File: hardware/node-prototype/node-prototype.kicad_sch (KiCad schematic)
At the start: 0 parts

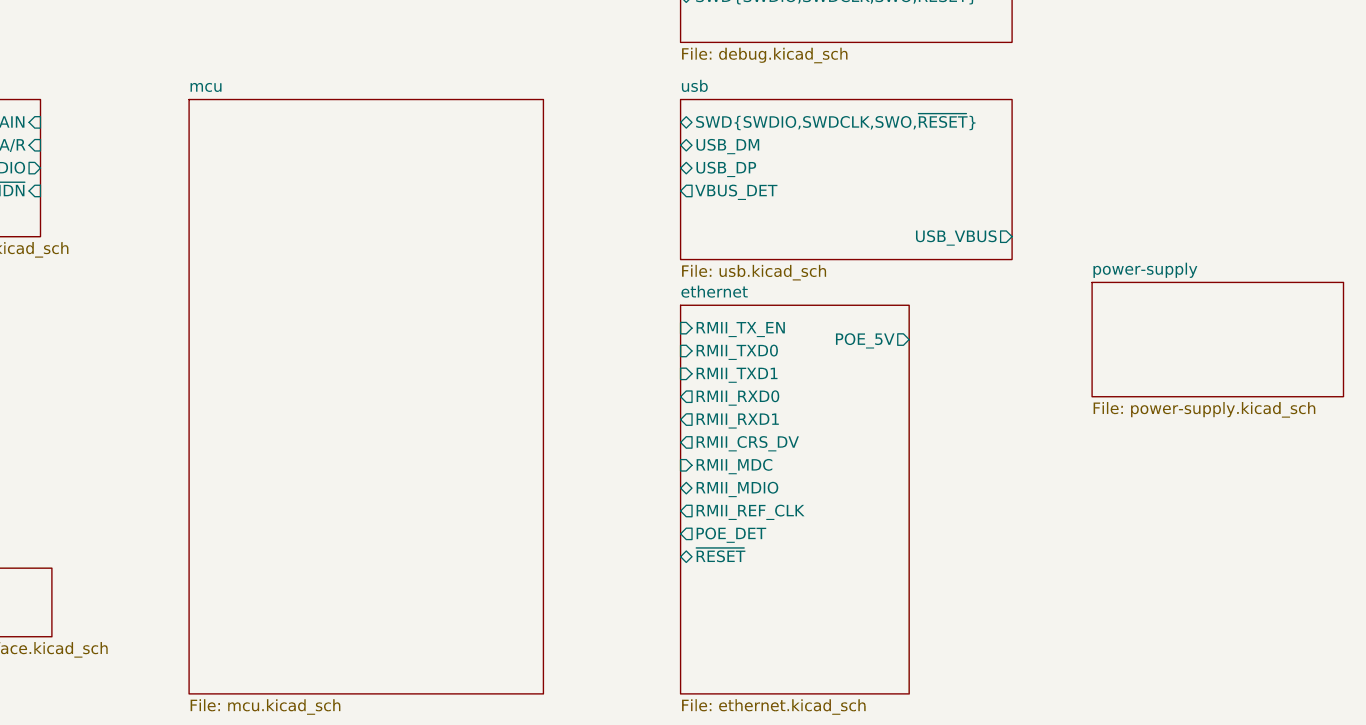
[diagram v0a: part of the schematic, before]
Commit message: Import labels in root sheet
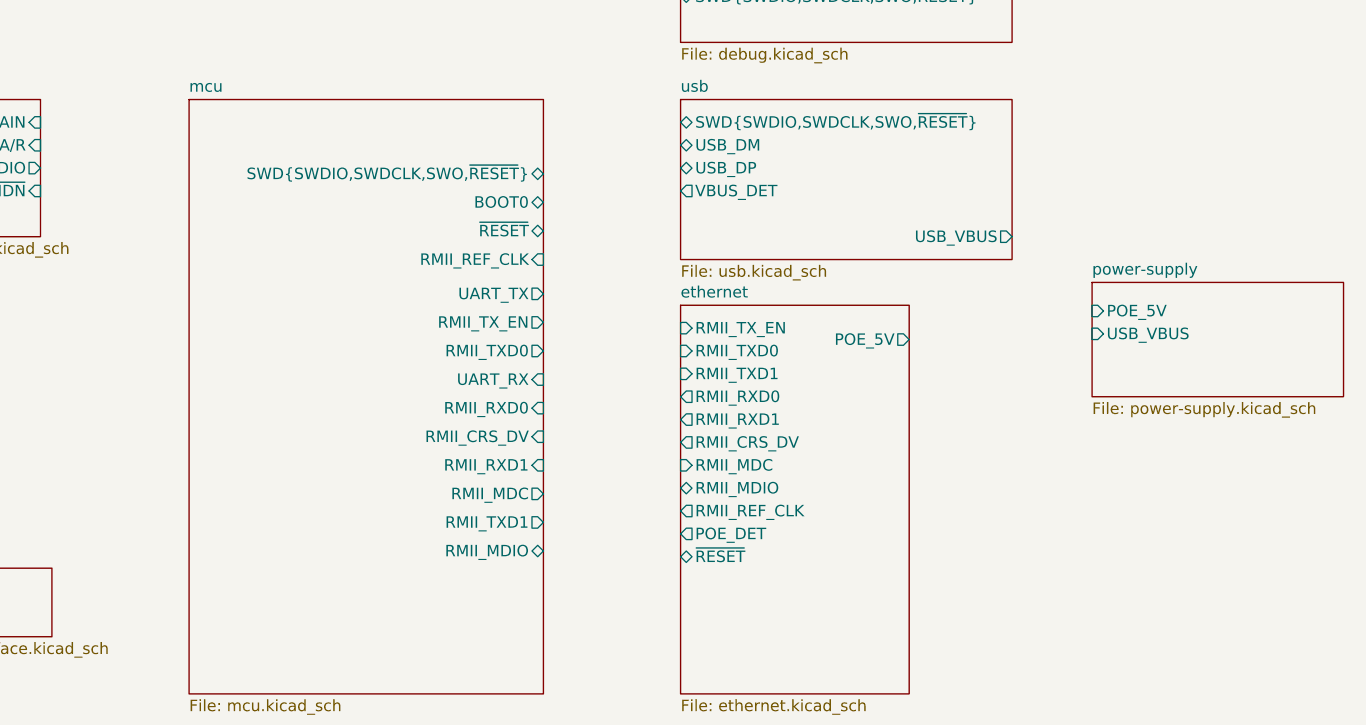
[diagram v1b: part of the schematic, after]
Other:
- sheet mcu ports: added BOOT0, RMII_CRS_DV, RMII_MDC, RMII_MDIO, RMII_REF_CLK, RMII_RXD0, RMII_RXD1, RMII_TXD0, RMII_TXD1, RMII_TX_EN, SWD{SWDIO,SWDCLK,SWO,~{RESET}}, UART_RX, UART_TX, ~{RESET}; removed none
- sheet power-supply ports: added POE_5V, USB_VBUS; removed none
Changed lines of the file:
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@@
       (effects (font (size 1.27 1.27)) (justify left top))
+    )
+    (pin "POE_5V" input (at 198.12 71.755 180)
+      (effects (font (size 1.27 1.27)) (justify left))
+    )
+    (pin "USB_VBUS" input (at 198.12 74.295 180)
+      (effects (font (size 1.27 1.27)) (justify left))
     )
     (instances
@@
       (effects (font (size 1.27 1.27)) (justify left top))
     )
+    (pin "SWD{SWDIO,SWDCLK,SWO,~{RESET}}" bidirectional (at 137.16 56.515 0)
+      (effects (font (size 1.27 1.27)) (justify right))
+    )
+    (pin "BOOT0" bidirectional (at 137.16 59.69 0)
+      (effects (font (size 1.27 1.27)) (justify right))
+    )
+    (pin "~{RESET}" bidirectional (at 137.16 62.865 0)
+      (effects (font (size 1.27 1.27)) (justify right))
+    )
+    (pin "RMII_REF_CLK" input (at 137.16 66.04 0)
+      (effects (font (size 1.27 1.27)) (justify right))
+    )
+    (pin "UART_TX" output (at 137.16 69.85 0)
+      (effects (font (size 1.27 1.27)) (justify right))
+    )
+    (pin "RMII_TX_EN" output (at 137.16 73.025 0)
+      (effects (font (size 1.27 1.27)) (justify right))
+    )
+    (pin "RMII_TXD0" output (at 137.16 76.2 0)
+      (effects (font (size 1.27 1.27)) (justify right))
+    )
+    (pin "UART_RX" input (at 137.16 79.375 0)
+      (effects (font (size 1.27 1.27)) (justify right))
+    )
+    (pin "RMII_RXD0" input (at 137.16 82.55 0)
+      (effects (font (size 1.27 1.27)) (justify right))
+    )
+    (pin "RMII_CRS_DV" input (at 137.16 85.725 0)
+      (effects (font (size 1.27 1.27)) (justify right))
+    )
+    (pin "RMII_RXD1" input (at 137.16 88.9 0)
+      (effects (font (size 1.27 1.27)) (justify right))
+    )
+    (pin "RMII_MDC" output (at 137.16 92.075 0)
+      (effects (font (size 1.27 1.27)) (justify right))
+    )
+    (pin "RMII_TXD1" output (at 137.16 95.25 0)
+      (effects (font (size 1.27 1.27)) (justify right))
+    )
+    (pin "RMII_MDIO" bidirectional (at 137.16 98.425 0)
+      (effects (font (size 1.27 1.27)) (justify right))
+    )
     (instances

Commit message: WIP on user interface
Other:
- sheet mcu ports: added USER_BTN, USER_LED_BLUE, USER_LED_RED; removed none
- sheet microphone ports: added MIC_AUDIO, MIC_A/R, MIC_GAIN, ~{MIC_SHDN}; removed AUDIO, A/R, GAIN, ~{SHDN}
- sheet user-interface ports: added BOOT0, USER_BTN, USER_LED_BLUE, USER_LED_RED, ~{RESET}; removed none
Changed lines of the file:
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@@
     (effects (font (size 1.27 1.27)) (justify left bottom))
   )
-  (sheet (at 63.5 100.33) (size 19.05 7.62) (fields_autoplaced)
+  (sheet (at 63.5 100.33) (size 19.05 29.845) (fields_autoplaced)
     (stroke (width 0.1524) (type solid))
     (fill (color 0 0 0 0.0000))
@@
       (effects (font (size 1.27 1.27)) (justify left bottom))
     )
-    (property "Sheetfile" "user-interface.kicad_sch" (at 63.5 108.5346 0)
-      (effects (font (size 1.27 1.27)) (justify left top))
+    (property "Sheetfile" "user-interface.kicad_sch" (at 63.5 130.7596 0)
+      (effects (font (size 1.27 1.27)) (justify left top))
+    )
+    (pin "BOOT0" output (at 82.55 107.315 0)
+      (effects (font (size 1.27 1.27)) (justify right))
+    )
+    (pin "USER_LED_RED" input (at 82.55 119.38 0)
+      (effects (font (size 1.27 1.27)) (justify right))
+    )
+    (pin "USER_BTN" output (at 82.55 109.855 0)
+      (effects (font (size 1.27 1.27)) (justify right))
+    )
+    (pin "USER_LED_BLUE" input (at 82.55 116.84 0)
+      (effects (font (size 1.27 1.27)) (justify right))
+    )
+    (pin "~{RESET}" output (at 82.55 104.775 0)
+      (effects (font (size 1.27 1.27)) (justify right))
     )
     (instances
@@
     )
   )
-  (sheet (at 60.96 48.26) (size 20.32 15.24) (fields_autoplaced)
-    (stroke (width 0.1524) (type solid))
-    (fill (color 0 0 0 0.0000))
-    (property "Sheetname" "microphone" (at 60.96 47.5484 0)
-      (effects (font (size 1.27 1.27)) (justify left bottom))
-    )
-    (property "Sheetfile" "microphone.kicad_sch" (at 60.96 64.0846 0)
-      (effects (font (size 1.27 1.27)) (justify left top))
-    )
-    (pin "GAIN" input (at 81.28 50.8 0)
-      (effects (font (size 1.27 1.27)) (justify right))
-    )
-    (pin "A{slash}R" input (at 81.28 53.34 0)
-      (effects (font (size 1.27 1.27)) (justify right))
-    )
-    (pin "AUDIO" output (at 81.28 55.88 0)
-      (effects (font (size 1.27 1.27)) (justify right))
-    )
-    (pin "~{SHDN}" input (at 81.28 58.42 0)
-      (effects (font (size 1.27 1.27)) (justify right))
+  (sheet (at 62.23 46.99) (size 20.32 38.1) (fields_autoplaced)
+    (stroke (width 0.1524) (type solid))
+    (fill (color 0 0 0 0.0000))
+    (property "Sheetname" "microphone" (at 62.23 46.2784 0)
+      (effects (font (size 1.27 1.27)) (justify left bottom))
+    )
+    (property "Sheetfile" "microphone.kicad_sch" (at 62.23 85.6746 0)
+      (effects (font (size 1.27 1.27)) (justify left top))
+    )
+    (pin "MIC_GAIN" input (at 62.23 52.07 180)
+      (effects (font (size 1.27 1.27)) (justify left))
+    )
+    (pin "MIC_AUDIO" output (at 62.23 49.53 180)
+      (effects (font (size 1.27 1.27)) (justify left))
+    )
+    (pin "~{MIC_SHDN}" input (at 62.23 54.61 180)
+      (effects (font (size 1.27 1.27)) (justify left))
+    )
+    (pin "MIC_A{slash}R" input (at 62.23 57.15 180)
+      (effects (font (size 1.27 1.27)) (justify left))
     )
     (instances
@@
       (effects (font (size 1.27 1.27)) (justify left top))
     )
-    (pin "SWD{SWDIO,SWDCLK,SWO,~{RESET}}" bidirectional (at 137.16 56.515 0)
-      (effects (font (size 1.27 1.27)) (justify right))
-    )
-    (pin "BOOT0" bidirectional (at 137.16 59.69 0)
-      (effects (font (size 1.27 1.27)) (justify right))
-    )
-    (pin "~{RESET}" bidirectional (at 137.16 62.865 0)
-      (effects (font (size 1.27 1.27)) (justify right))
-    )
-    (pin "RMII_REF_CLK" input (at 137.16 66.04 0)
-      (effects (font (size 1.27 1.27)) (justify right))
-    )
-    (pin "UART_TX" output (at 137.16 69.85 0)
-      (effects (font (size 1.27 1.27)) (justify right))
-    )
-    (pin "RMII_TX_EN" output (at 137.16 73.025 0)
-      (effects (font (size 1.27 1.27)) (justify right))
-    )
-    (pin "RMII_TXD0" output (at 137.16 76.2 0)
-      (effects (font (size 1.27 1.27)) (justify right))
-    )
-    (pin "UART_RX" input (at 137.16 79.375 0)
-      (effects (font (size 1.27 1.27)) (justify right))
-    )
-    (pin "RMII_RXD0" input (at 137.16 82.55 0)
-      (effects (font (size 1.27 1.27)) (justify right))
-    )
-    (pin "RMII_CRS_DV" input (at 137.16 85.725 0)
-      (effects (font (size 1.27 1.27)) (justify right))
-    )
-    (pin "RMII_RXD1" input (at 137.16 88.9 0)
-      (effects (font (size 1.27 1.27)) (justify right))
-    )
-    (pin "RMII_MDC" output (at 137.16 92.075 0)
-      (effects (font (size 1.27 1.27)) (justify right))
-    )
-    (pin "RMII_TXD1" output (at 137.16 95.25 0)
-      (effects (font (size 1.27 1.27)) (justify right))
-    )
-    (pin "RMII_MDIO" bidirectional (at 137.16 98.425 0)
-      (effects (font (size 1.27 1.27)) (justify right))
-    )
+    (pin "SWD{SWDIO,SWDCLK,SWO,~{RESET}}" bidirectional (at 137.16 73.66 0)
+      (effects (font (size 1.27 1.27)) (justify right))
+    )
+    (pin "BOOT0" input (at 137.16 51.435 0)
+      (effects (font (size 1.27 1.27)) (justify right))
+    )
+    (pin "~{RESET}" input (at 137.16 54.61 0)
+      (effects (font (size 1.27 1.27)) (justify right))
+    )
+    (pin "RMII_REF_CLK" input (at 137.16 76.2 0)
+      (effects (font (size 1.27 1.27)) (justify right))
+    )
+    (pin "UART_TX" output (at 137.16 80.01 0)
+      (effects (font (size 1.27 1.27)) (justify right))
+    )
+    (pin "RMII_TX_EN" output (at 137.16 83.185 0)
+      (effects (font (size 1.27 1.27)) (justify right))
+    )
+    (pin "RMII_TXD0" output (at 137.16 86.36 0)
+      (effects (font (size 1.27 1.27)) (justify right))
+    )
+    (pin "UART_RX" input (at 137.16 89.535 0)
+      (effects (font (size 1.27 1.27)) (justify right))
+    )
+    (pin "RMII_RXD0" input (at 137.16 92.71 0)
+      (effects (font (size 1.27 1.27)) (justify right))
+    )
+    (pin "RMII_CRS_DV" input (at 137.16 95.885 0)
+      (effects (font (size 1.27 1.27)) (justify right))
+    )
+    (pin "RMII_RXD1" input (at 137.16 99.06 0)
+      (effects (font (size 1.27 1.27)) (justify right))
+    )
+    (pin "RMII_MDC" output (at 137.16 102.235 0)
+      (effects (font (size 1.27 1.27)) (justify right))
+    )
+    (pin "RMII_TXD1" output (at 137.16 105.41 0)
+      (effects (font (size 1.27 1.27)) (justify right))
+    )
+    (pin "RMII_MDIO" bidirectional (at 137.16 108.585 0)
+      (effects (font (size 1.27 1.27)) (justify right))
+    )
+    (pin "USER_BTN" input (at 137.16 57.15 0)
+      (effects (font (size 1.27 1.27)) (justify right))
+    )
+    (pin "USER_LED_BLUE" output (at 137.16 62.23 0)
+      (effects (font (size 1.27 1.27)) (justify right))
+    )
+    (pin "USER_LED_RED" output (at 137.16 65.405 0)
+      (effects (font (size 1.27 1.27)) (justify right))
+    )

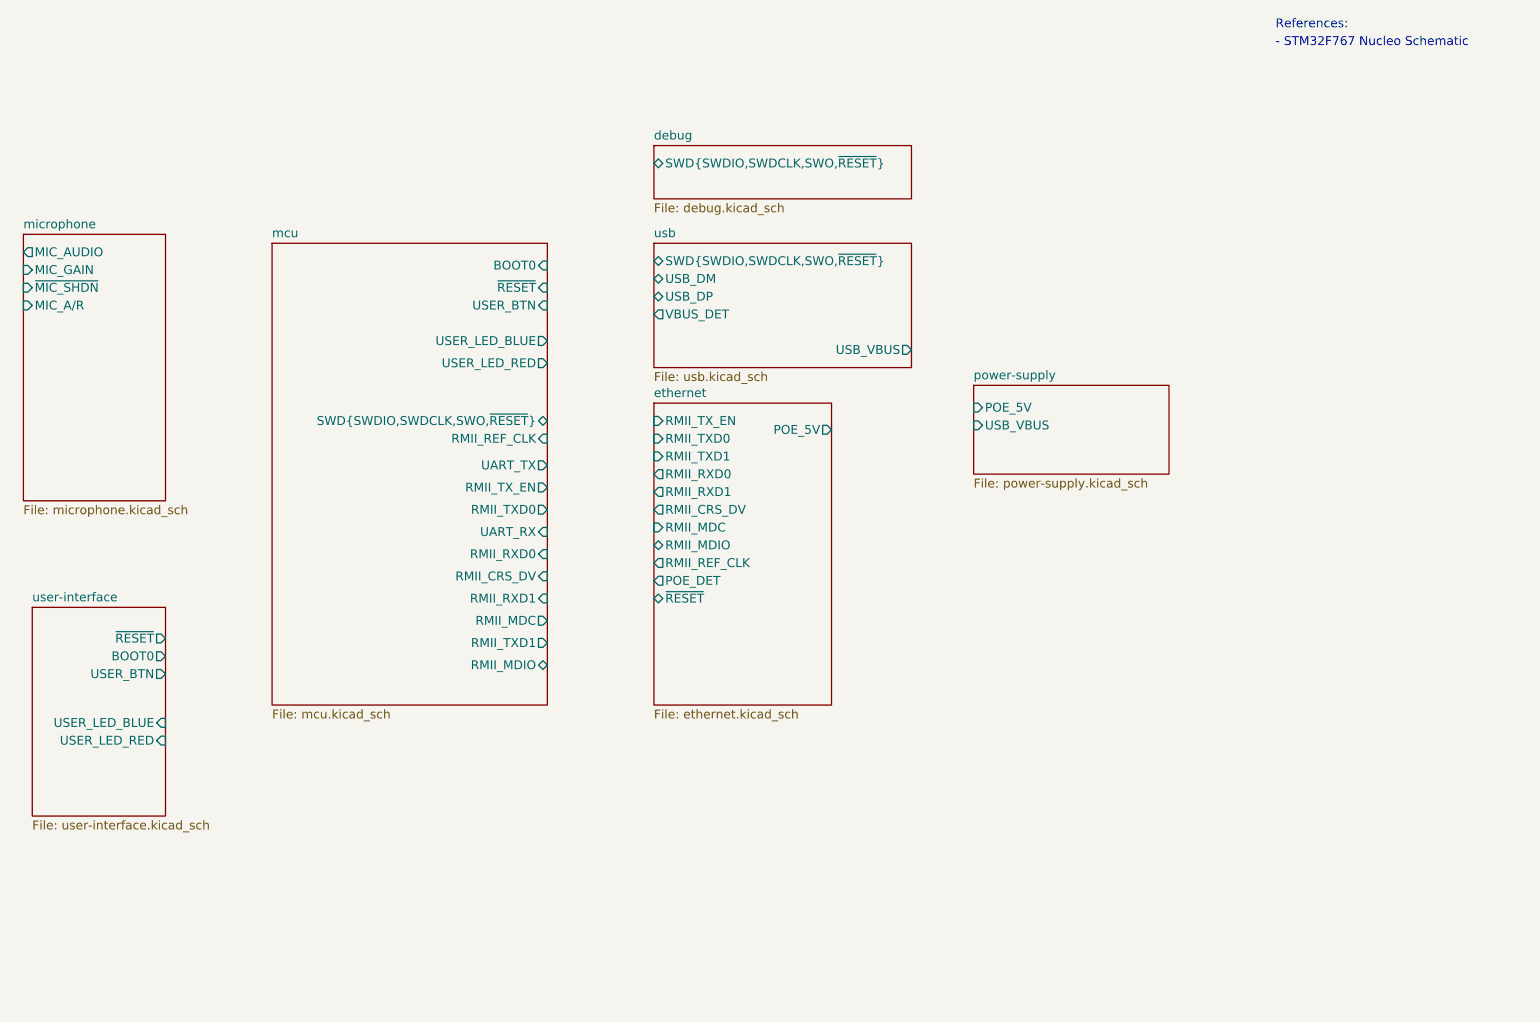
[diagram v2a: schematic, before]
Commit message: Plug schematic together
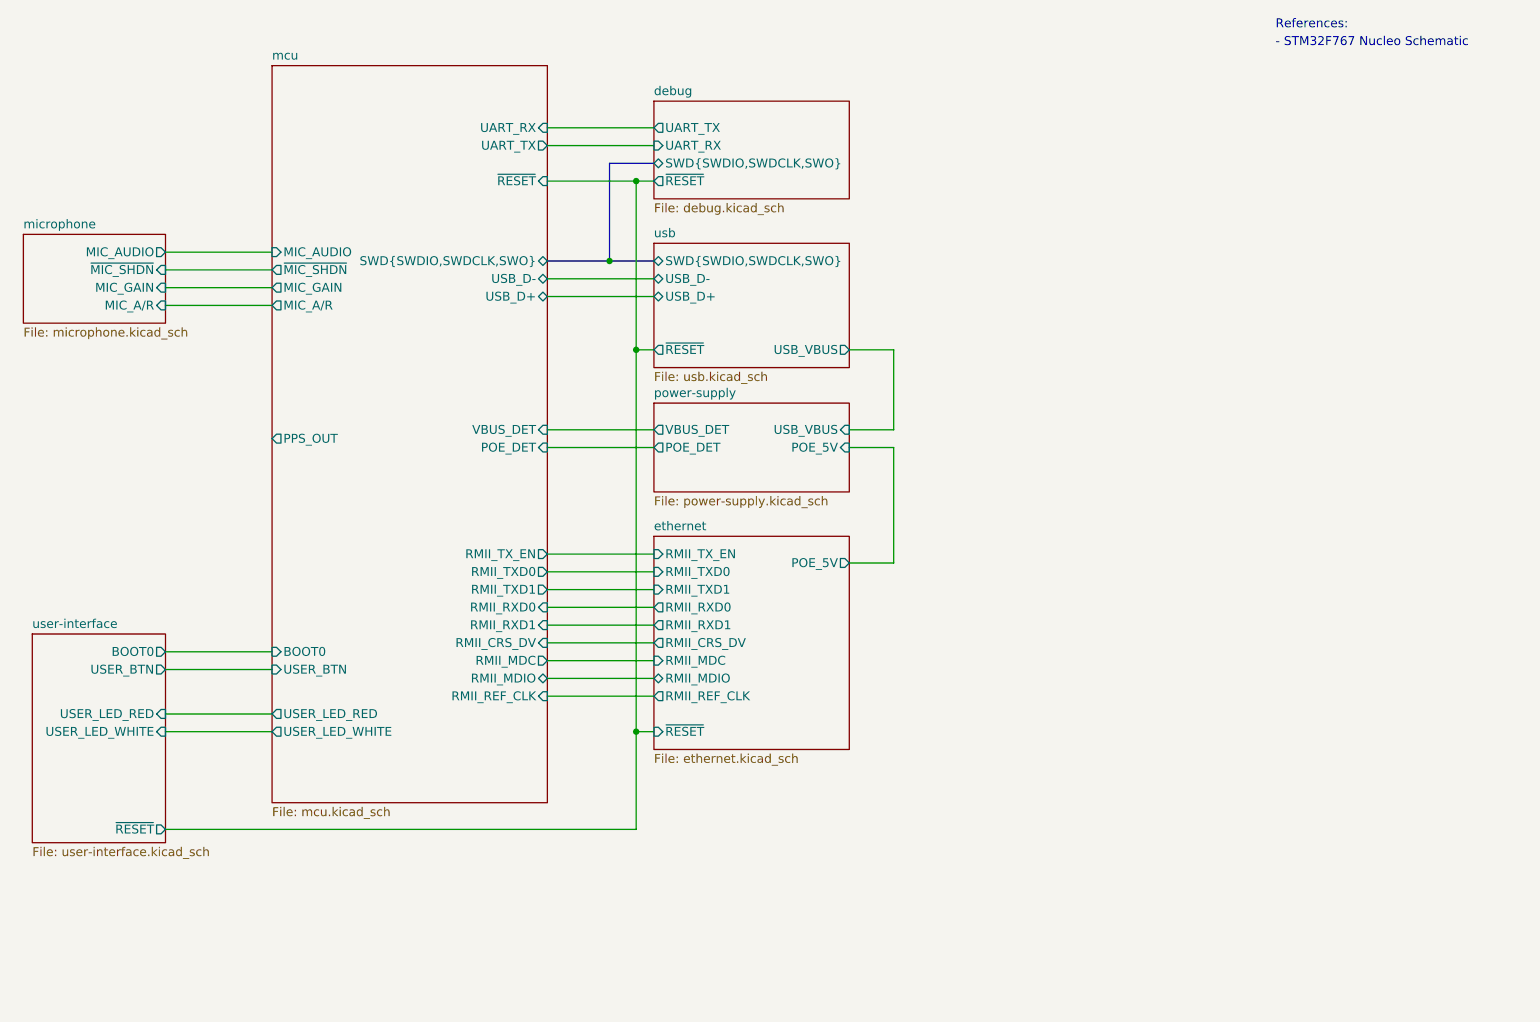
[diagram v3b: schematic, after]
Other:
- sheet debug ports: added SWD{SWDIO,SWDCLK,SWO}, UART_RX, UART_TX, ~{RESET}; removed SWD{SWDIO,SWDCLK,SWO,~{RESET}}
- sheet ethernet ports: added none; removed POE_DET
- sheet mcu ports: added MIC_AUDIO, MIC_A/R, MIC_GAIN, POE_DET, PPS_OUT, SWD{SWDIO,SWDCLK,SWO}, USB_D+, USB_D-, USER_LED_WHITE, VBUS_DET, ~{MIC_SHDN}; removed SWD{SWDIO,SWDCLK,SWO,~{RESET}}, USER_LED_BLUE
- sheet power-supply ports: added POE_DET, VBUS_DET; removed none
- sheet usb ports: added SWD{SWDIO,SWDCLK,SWO}, USB_D+, USB_D-, ~{RESET}; removed SWD{SWDIO,SWDCLK,SWO,~{RESET}}, USB_DM, USB_DP, VBUS_DET
- sheet user-interface ports: added USER_LED_WHITE; removed USER_LED_BLUE
